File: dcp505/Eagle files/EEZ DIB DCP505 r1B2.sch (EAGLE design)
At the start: 323 parts, among them IC1 LP2951, IC10 OPA4197IDR, IC11 MC33272ADR2G, IC12 MC33274ADR2G, IC13 74HC4066PW, IC14 74AUP1G74DC.125, IC15 MCP23S17-E/SS, IC16 REF5025AIDG4, IC17 DAC8552IDGKTG4, IC18 SN74LVC1G3157, IC19 ADS1120IPWR, IC2 SI8641AB-B-IS1, IC20 LM339D, IC21 LM211PWR, IC3 SN74LVC1G139DCUR, IC4 MC79L05, IC5 SI8641AB-B-IS1, IC6 AT24C02D-SSHM-T, IC7 TC77-5.0MCTTR, IC8 TL072D, IC9 MC33274ADR2G, J1 FCR7350R, J2 FCR7350B, K1 G6K-2F-5DC, Q1 IRFP250N, Q10 MMBT5551, Q11 PSMN0R9-25YLC, Q12 PSMN0R9-25YLC, Q13 PSMN0R9-25YLC, Q14 2N7002, Q15 2N7002, Q16 MMBT5401, Q17 MMBT5401, Q18 2N7002, Q19 IRLML2246TRPBF, Q2 BCP56-16.115, Q20 BTA26-600, Q21 2N7002, Q22 MMBT5551, Q23 2N7002, Q24 2N7002, Q25 MMBT5551, Q26 MMBT5551, Q27 MMBT5401, Q28 MMBT5551, Q29 MMBT5551, Q3 BC856C, Q30 BSS84P, Q31 2N7002, Q4 BCP56-16.115, Q5 STF10P6F6 or IRF9Z24 or FQPF2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, Q6 BCP56-16.115, Q7 MMBT5401, Q8 MMBT5401, Q9 MMBT5551, X1 ZL263-26DG, X2 22-05-7085, X3 39-30-3035, X4 1844249, X5 ZL263-20DG

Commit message: small PCB optimizations
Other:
- note added: "-"
- note added: "PCB inductor ~1.1 uH !"
- note removed: "Extra Cout"
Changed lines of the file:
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@@
 <setting verticaltext="up"/>
 </settings>
-<grid distance="0.1" unitdist="inch" unit="inch" style="lines" multiple="1" display="no" altdistance="0.01" altunitdist="inch" altunit="inch"/>
+<grid distance="25" unitdist="mil" unit="mil" style="lines" multiple="4" display="no" altdistance="0.01" altunitdist="inch" altunit="inch"/>
 <layers>
 <layer number="1" name="Top" color="4" fill="1" visible="no" active="no"/>
@@
 <text x="46.99" y="115.57" size="1.4224" layer="104">Require SPI_MODE0</text>
 <text x="252.73" y="131.445" size="1.6764" layer="103" align="bottom-center">Output</text>
-<text x="252.73" y="128.905" size="1.6764" layer="103" align="bottom-center">Output</text>
+<text x="252.73" y="128.905" size="1.6764" layer="103" align="bottom-center">Input</text>
 <text x="213.36" y="144.145" size="1.6764" layer="103" align="bottom-center">6</text>
 <text x="213.36" y="136.525" size="1.6764" layer="103" align="bottom-center">9</text>
@@
 <text x="218.44" y="123.825" size="1.6764" layer="103">Current range 50 mA</text>
 <text x="213.36" y="133.985" size="1.6764" layer="103" align="bottom-center">10</text>
-<text x="252.73" y="126.365" size="1.6764" layer="103" align="bottom-center">Output</text>
+<text x="252.73" y="126.365" size="1.6764" layer="103" align="bottom-center">Input</text>
 <text x="188.595" y="107.315" size="1.27" layer="100">+2.5 V</text>
 <text x="213.36" y="121.285" size="1.6764" layer="103" align="bottom-center">15</text>
-<text x="218.44" y="121.285" size="1.6764" layer="103">Extra Cout</text>
-<text x="252.73" y="121.285" size="1.6764" layer="103" align="bottom-center">Output</text>
+<text x="218.44" y="121.285" size="1.6764" layer="103">-</text>
+<text x="252.73" y="121.285" size="1.6764" layer="103" align="bottom-center">-</text>
 <text x="218.44" y="141.605" size="1.6764" layer="103">OE coupled LED</text>
 <text x="213.36" y="131.445" size="1.6764" layer="103" align="bottom-center">11</text>
@@
 <text x="213.36" y="126.365" size="1.6764" layer="103" align="bottom-center">13</text>
 <text x="213.36" y="123.825" size="1.6764" layer="103" align="bottom-center">14</text>
-<text x="252.73" y="123.825" size="1.6764" layer="103" align="bottom-center">Output</text>
+<text x="252.73" y="123.825" size="1.6764" layer="103" align="bottom-center">Input</text>
 <text x="252.73" y="136.525" size="1.6764" layer="103" align="bottom-center">Output</text>
 <text x="119.38" y="12.065" size="1.6764" layer="103">AIN0</text>
@@
 <rectangle x1="141.605" y1="119.38" x2="148.59" y2="126.365" layer="97"/>
 <wire x1="119.38" y1="83.82" x2="119.38" y2="172.72" width="0.1524" layer="97" style="shortdash"/>
+<wire x1="243.84" y1="121.92" x2="240.665" y2="121.92" width="0.1524" layer="100"/>
+<polygon width="0.1524" layer="100">
+<vertex x="240.665" y="121.92"/>
+<vertex x="241.935" y="122.2375"/>
+<vertex x="241.935" y="121.6025"/>
+</polygon>
+<text x="244.475" y="120.3325" size="1.27" layer="100">PCB inductor
+~1.1 uH !</text>
+<wire x1="237.49" y1="127" x2="240.03" y2="127" width="0.1524" layer="100"/>
+<wire x1="240.03" y1="127" x2="240.03" y2="115.57" width="0.1524" layer="100"/>
+<wire x1="240.03" y1="115.57" x2="237.49" y2="115.57" width="0.1524" layer="100"/>
+<wire x1="237.49" y1="115.57" x2="237.49" y2="127" width="0.1524" layer="100"/>
 </plain>
 <instances>
@@
 <label x="243.84" y="114.3" size="1.27" layer="102" xref="yes"/>
 <pinref part="R110" gate="G$1" pin="1"/>
-<wire x1="238.76" y1="127" x2="238.76" y2="124.46" width="0.4064" layer="91"/>
-<wire x1="238.76" y1="114.3" x2="238.76" y2="124.46" width="0.1524" layer="91"/>
+<wire x1="238.76" y1="127" x2="238.76" y2="114.3" width="0.4064" layer="91"/>
 </segment>
 </net>
@@
 </schematic>
 </drawing>
+<compatibility>
+<note version="6.3" minversion="6.2.2" severity="warning">
+Since Version 6.2.2 text objects can contain more than one line,
+which will not be processed correctly with this version.
+</note>
+</compatibility>
 </eagle>

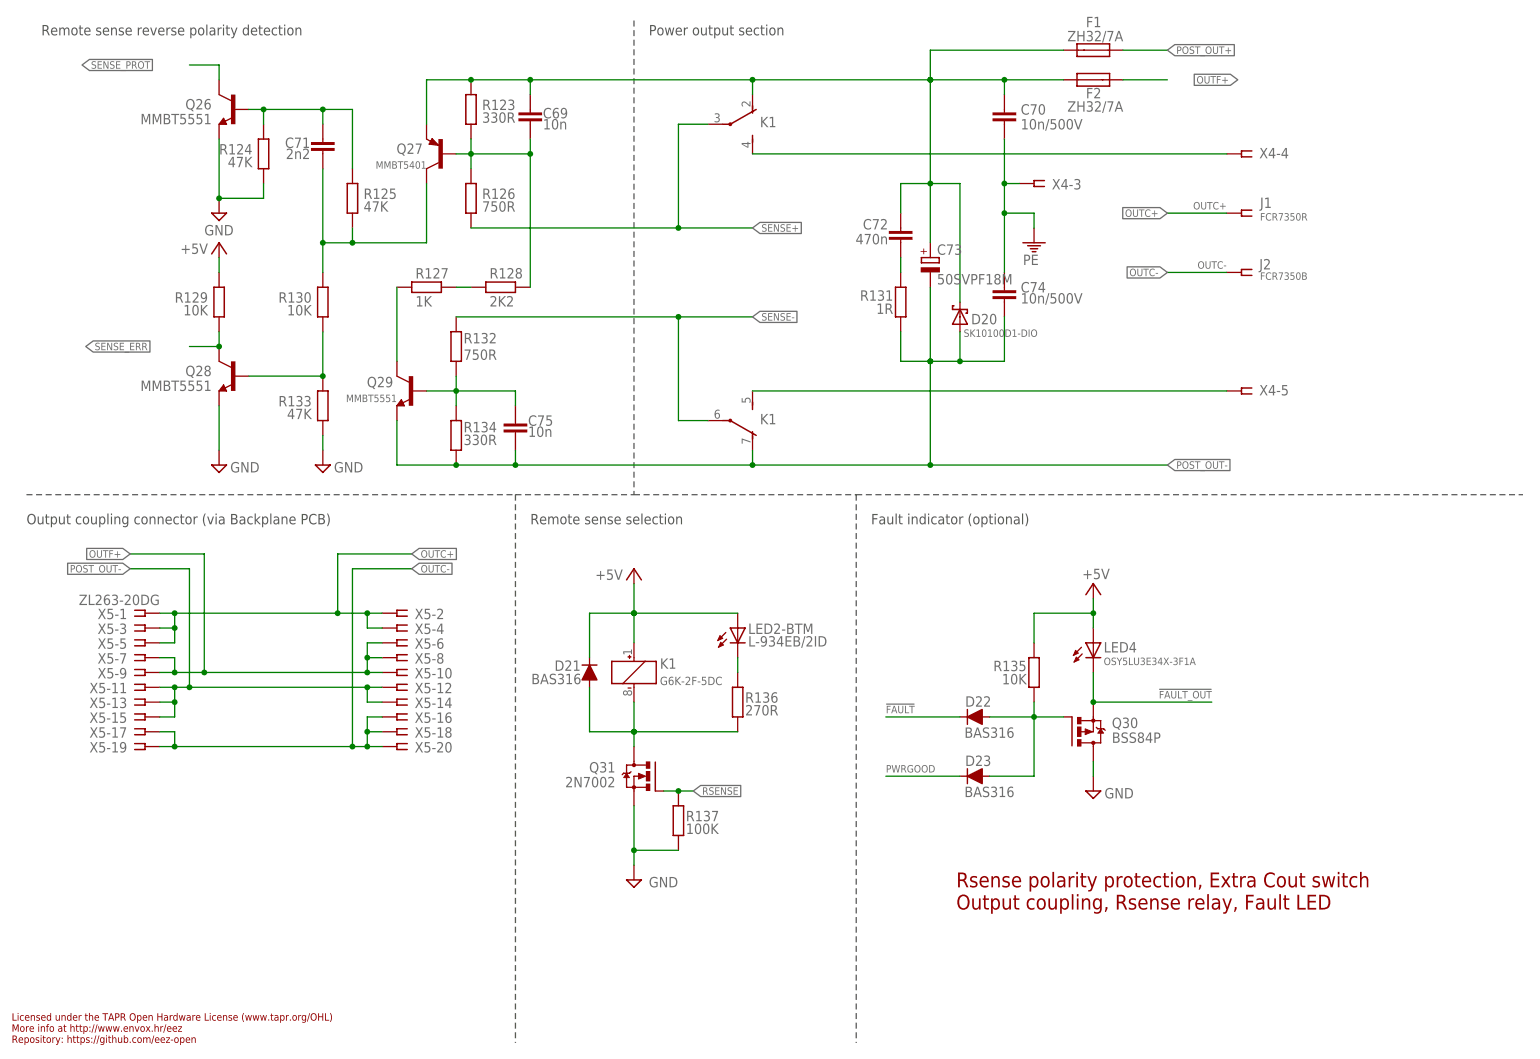
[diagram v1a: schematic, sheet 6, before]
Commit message: DCP505: replaced temperature sensor (IC7)
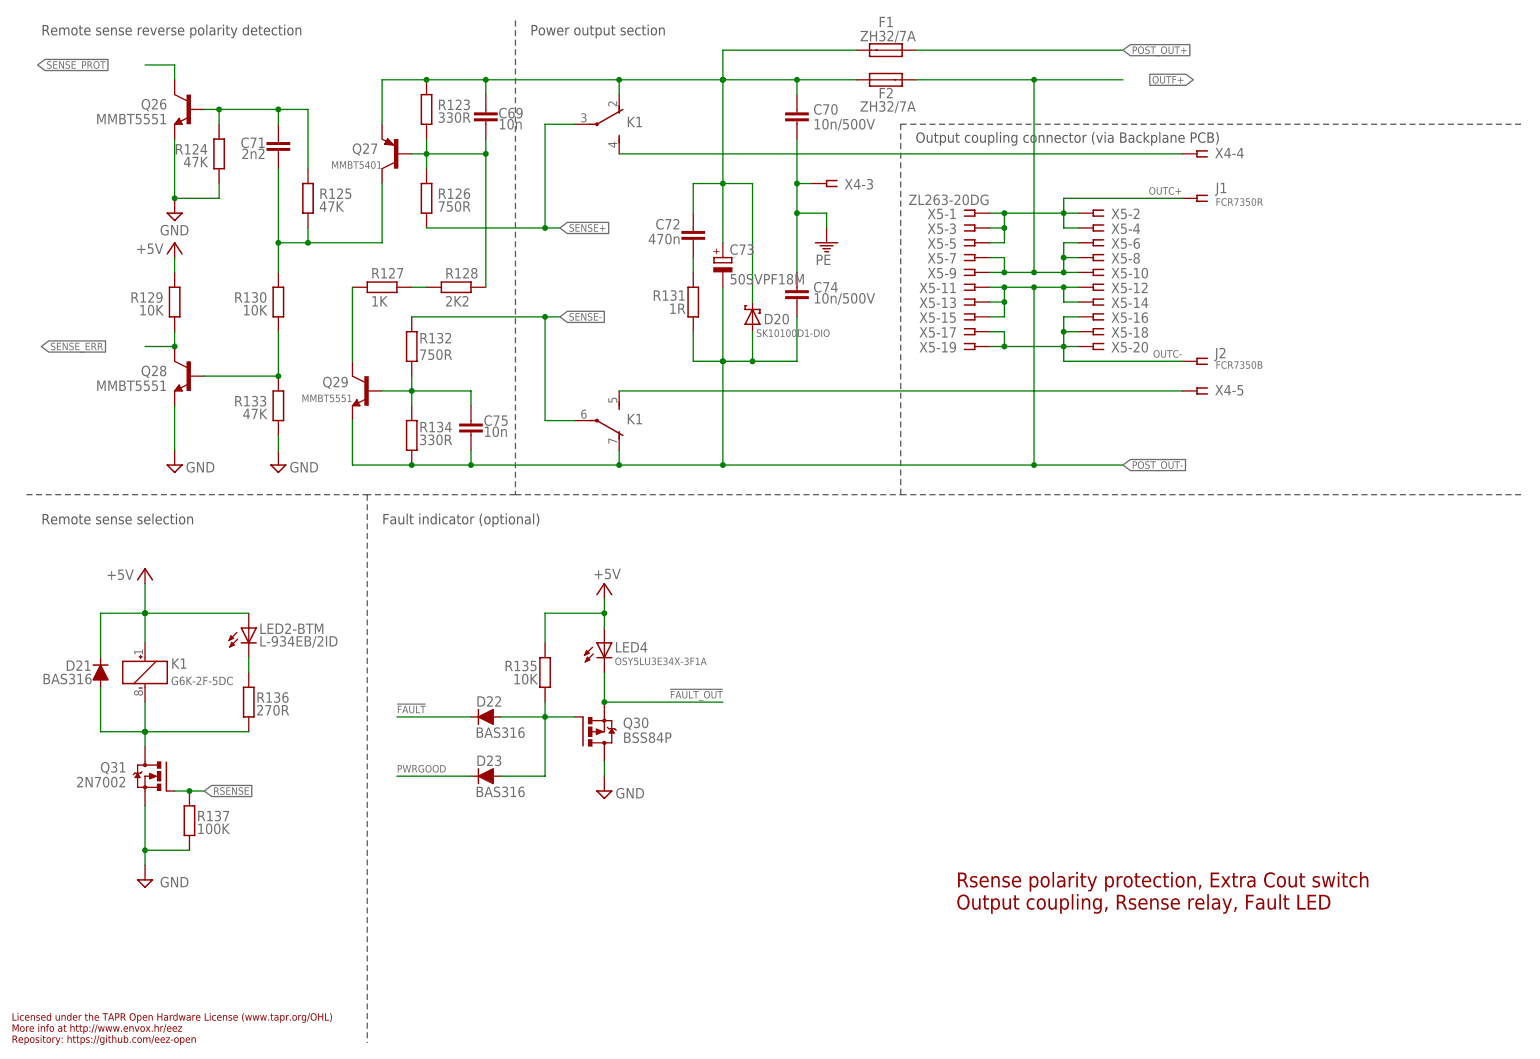
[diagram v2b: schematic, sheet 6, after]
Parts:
- added JP4: JP3-CUT, EEZ_Lib1:JP3-CUT
- IC7: value TC77-5.0MCTTR -> TMP1075AIDGK; device EEZ_Lib1:TC77 -> EEZ_Lib1:TMPX75DGK
- JP2: value JP2-CUT -> JP3-CUT; device EEZ_Lib1:JP2-CUT -> EEZ_Lib1:JP3-CUT
- JP3: value JP3-CUT -> JP2-CUT; device EEZ_Lib1:JP3-CUT -> EEZ_Lib1:JP2-CUT
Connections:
- removed net CS_TEMP: IC7.!CS, RN1-3.2
- removed net N$25: IC3.Y2, RN1-3.1
- new net N$64: JP2.NO, X2-7.1
- new net N$66: JP2.NC, X2-8.1
- net !DRDY: now also JP4.NC; no longer JP3.NC
- net +3V3: now also C17.1, IC7.V+
- net +5V: no longer C17.1, IC7.VDD
- net DIB_A0: now also IC7.A0
- net DIB_A1: now also IC7.A1
- net DIB_A2: now also IC7.A2
- net DIB_NFAULT: now also IC7.ALERT
- net DIB_SCL: now also IC7.SCL
- net DIB_SDA: now also IC7.SDA
- net GND: no longer C17.2, IC7.GND
- net GNDIO: now also C17.2, IC7.GND
- net IRQ: now also JP4.COM; no longer JP3.COM
- net MISO: no longer IC7.SI/O
- net N$3: now also JP4.NO; no longer JP3.NO
- net N$45: now also JP3.2; no longer JP2.2
- net PREG_IN+: now also JP2.COM; no longer X2-8.1
- net PRE_OE: now also JP3.1; no longer JP2.1
- net SCLK: no longer IC7.SCLK
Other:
- note added: "I2C temperature sensor"
- note removed: "SPI temperature sensor"
- moved on the sheet: C10, C11, C12, C13, C16, C17, C2, C3, C4, C5, C69, C70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

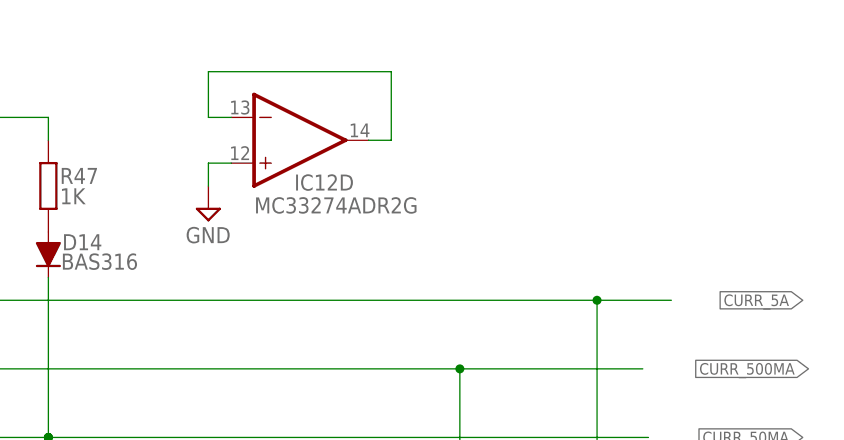
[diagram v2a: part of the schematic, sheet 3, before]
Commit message: fix PCB inductor dimensions
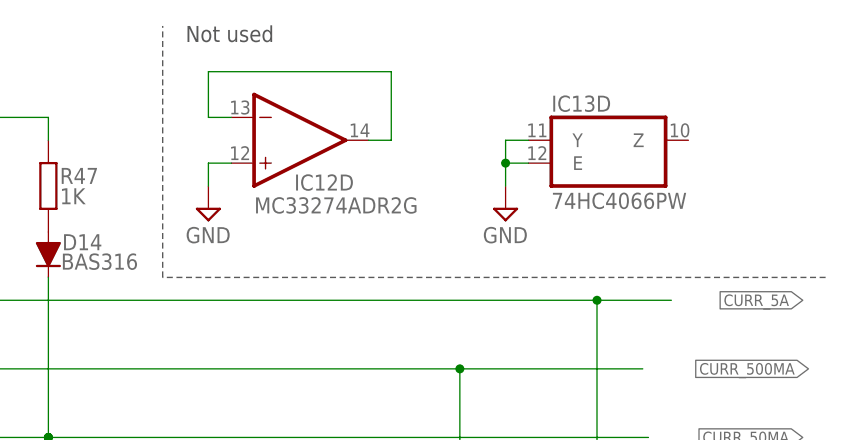
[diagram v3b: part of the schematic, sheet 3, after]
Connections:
- net GND: now also IC13D.E, IC13D.Y
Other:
- note added: "Not used"
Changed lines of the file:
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@@
 <part name="IC7" library="EEZ_Lib1" deviceset="TMPX75" device="DGK" value="TMP1075AIDGK"/>
 <part name="JP2" library="EEZ_Lib1" deviceset="JP3-CUT" device=""/>
+<part name="SUPPLY15" library="supply2" deviceset="GND" device=""/>
 </parts>
 <sheets>
@@
 <text x="154.94" y="48.895" size="1.27" layer="100">-2.5 V</text>
 <text x="133.35" y="83.185" size="1.27" layer="103" rot="MR0">See Note 3.1</text>
+<text x="190.5" y="177.8" size="1.778" layer="97" rot="MR180">Not used</text>
+<wire x1="187.96" y1="149.86" x2="187.96" y2="177.8" width="0.1524" layer="97" style="shortdash"/>
+<wire x1="261.62" y1="149.86" x2="187.96" y2="149.86" width="0.1524" layer="97" style="shortdash"/>
 </plain>
 <instances>
@@
 <attribute name="VALUE" x="42.545" y="90.17" size="1.778" layer="96" rot="R180"/>
 </instance>
+<instance part="IC13" gate="D" x="236.22" y="165.1"/>
+<instance part="SUPPLY15" gate="GND" x="226.06" y="157.48" smashed="yes">
+<attribute name="VALUE" x="223.52" y="153.67" size="1.778" layer="96"/>
+</instance>
 </instances>
 <busses>
@@
 <pinref part="SUPPLY69" gate="GND" pin="GND"/>
 </segment>
+<segment>
+<pinref part="IC13" gate="D" pin="E"/>
+<wire x1="228.6" y1="162.56" x2="226.06" y2="162.56" width="0.1524" layer="91"/>
+<wire x1="226.06" y1="162.56" x2="226.06" y2="160.02" width="0.1524" layer="91"/>
+<pinref part="IC13" gate="D" pin="Y"/>
+<wire x1="228.6" y1="165.1" x2="226.06" y2="165.1" width="0.1524" layer="91"/>
+<wire x1="226.06" y1="165.1" x2="226.06" y2="162.56" width="0.1524" layer="91"/>
+<junction x="226.06" y="162.56"/>
+<pinref part="SUPPLY15" gate="GND" pin="GND"/>
+</segment>
 </net>
